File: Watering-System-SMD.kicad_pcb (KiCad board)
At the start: 2 copper layers, 76 x 30 mm, 24 parts, among them CON1 AVR-ISP-6, J1 Screw_Terminal_1x02, J2 CONN_01X04_MALE, J3 Screw_Terminal_1x04, J4 Screw_Terminal_1x02, M3 MountingHole_3.2mm_M3, Q1 MMBF170, Q2 2N7002, U1 MCP1703A-3302/MB, U2 ATTINY84-20SSU, U3 ESP-01

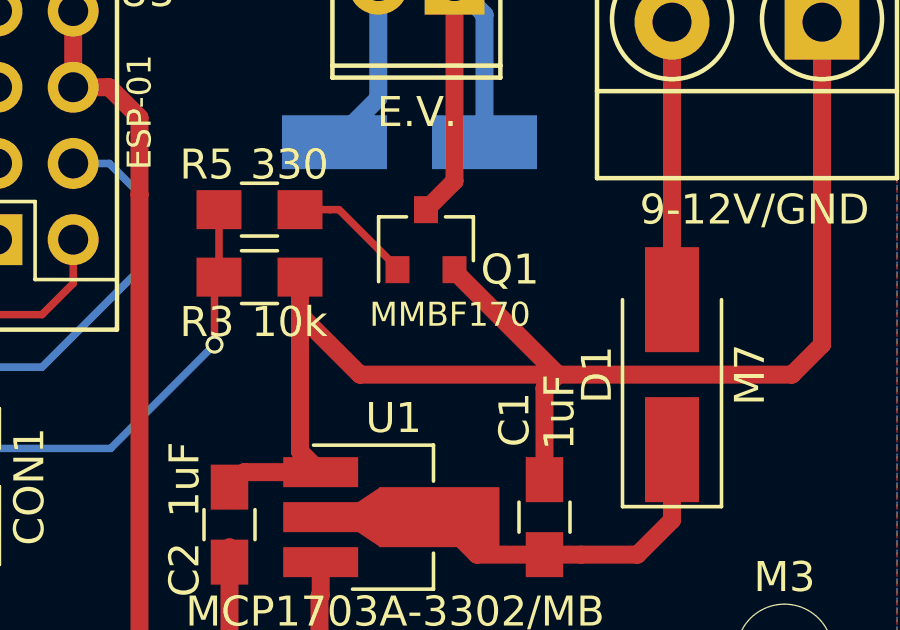
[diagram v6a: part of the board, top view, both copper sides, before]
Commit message: MOSFET changed
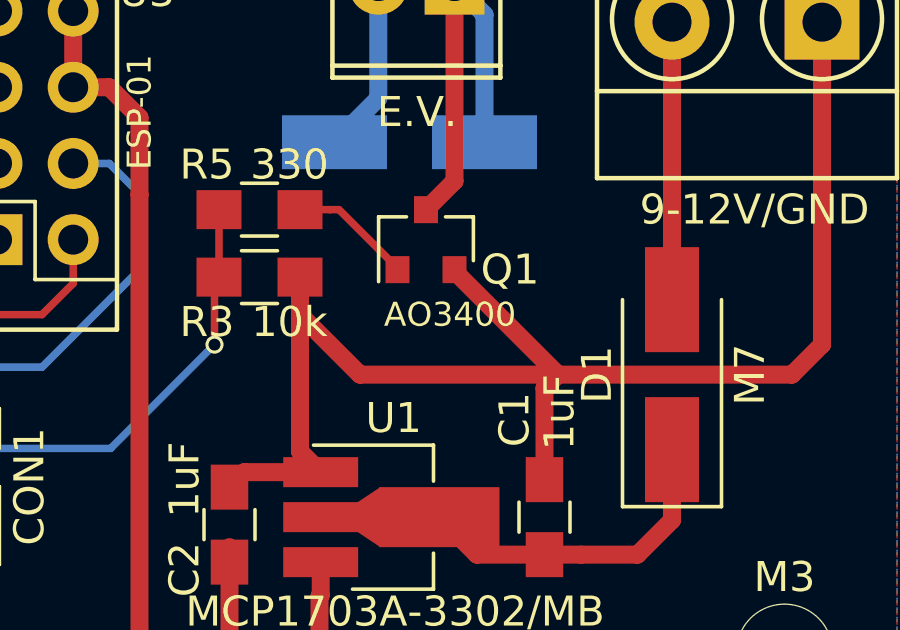
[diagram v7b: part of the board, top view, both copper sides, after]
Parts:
- Q1: value MMBF170 -> AO3400
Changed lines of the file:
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@@
-(kicad_pcb (version 4) (host pcbnew 4.0.6-e0-6349~53~ubuntu16.04.1)
+(kicad_pcb (version 4) (host pcbnew 4.0.7-e2-6376~58~ubuntu16.04.1)
   (general
     (links 51)
     (no_connects 0)
-    (area 52.924999 68.924999 129.075001 99.075001)
+    (area 36.72143 63.678571 145.202382 108.7)
     (thickness 1.6)
     (drawings 13)
@@
       (effects (font (size 1 1) (thickness 0.15)))
     )
-    (fp_text value MMBF170 (at -2.5 0.8 180) (layer F.SilkS)
+    (fp_text value AO3400 (at -2.5 0.8 180) (layer F.SilkS)
       (effects (font (size 0.8 0.8) (thickness 0.15)))
     )
